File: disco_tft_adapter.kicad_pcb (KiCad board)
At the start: 4 copper layers, 127 x 60 mm, 14 parts, among them J1 QTH-030-02-L-D-A, J2 F31L-1A7H1-11030

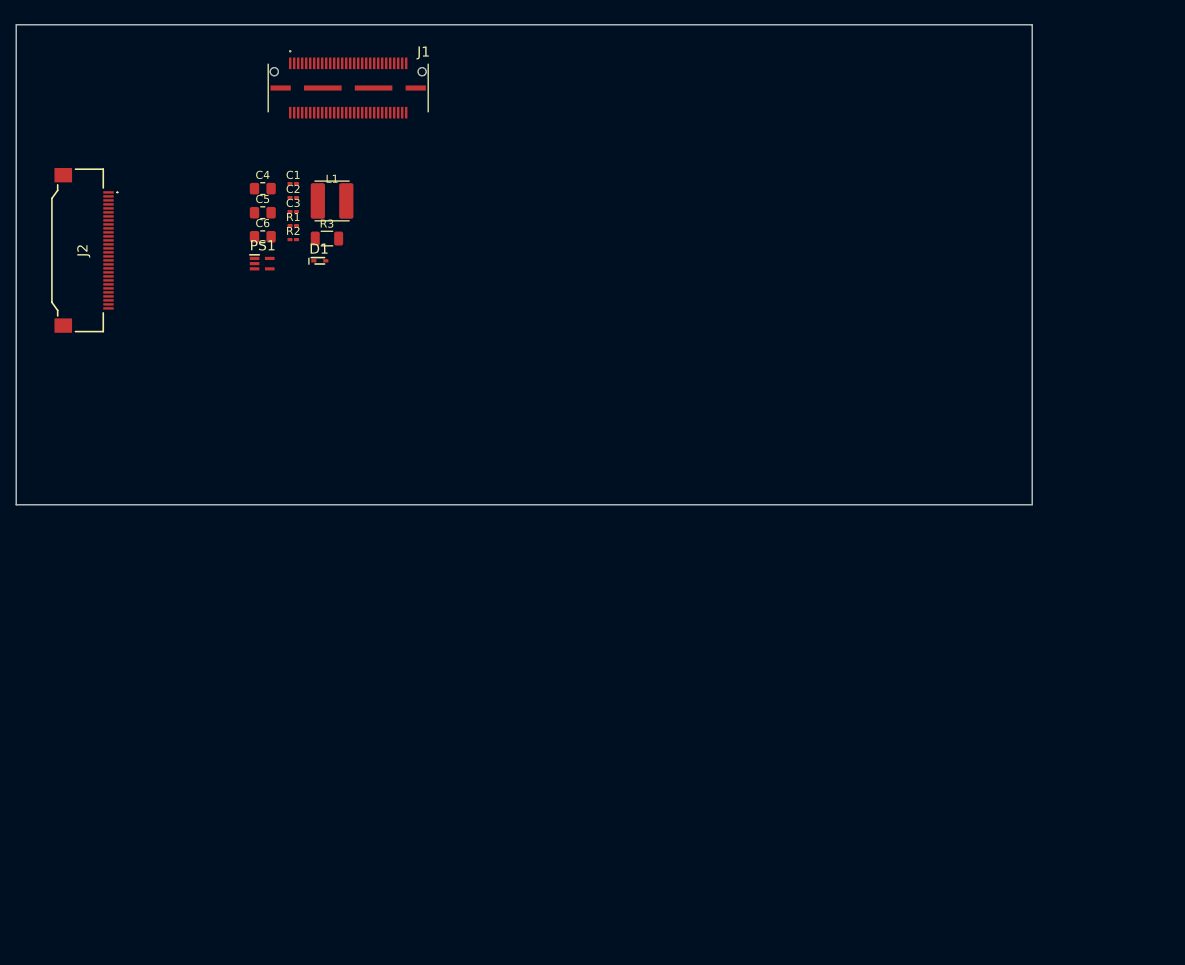
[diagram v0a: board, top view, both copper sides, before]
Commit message: [layout] add: stitching vias, planes updated, routed buck converter for LED BL, added power labels to buck converter in schematics
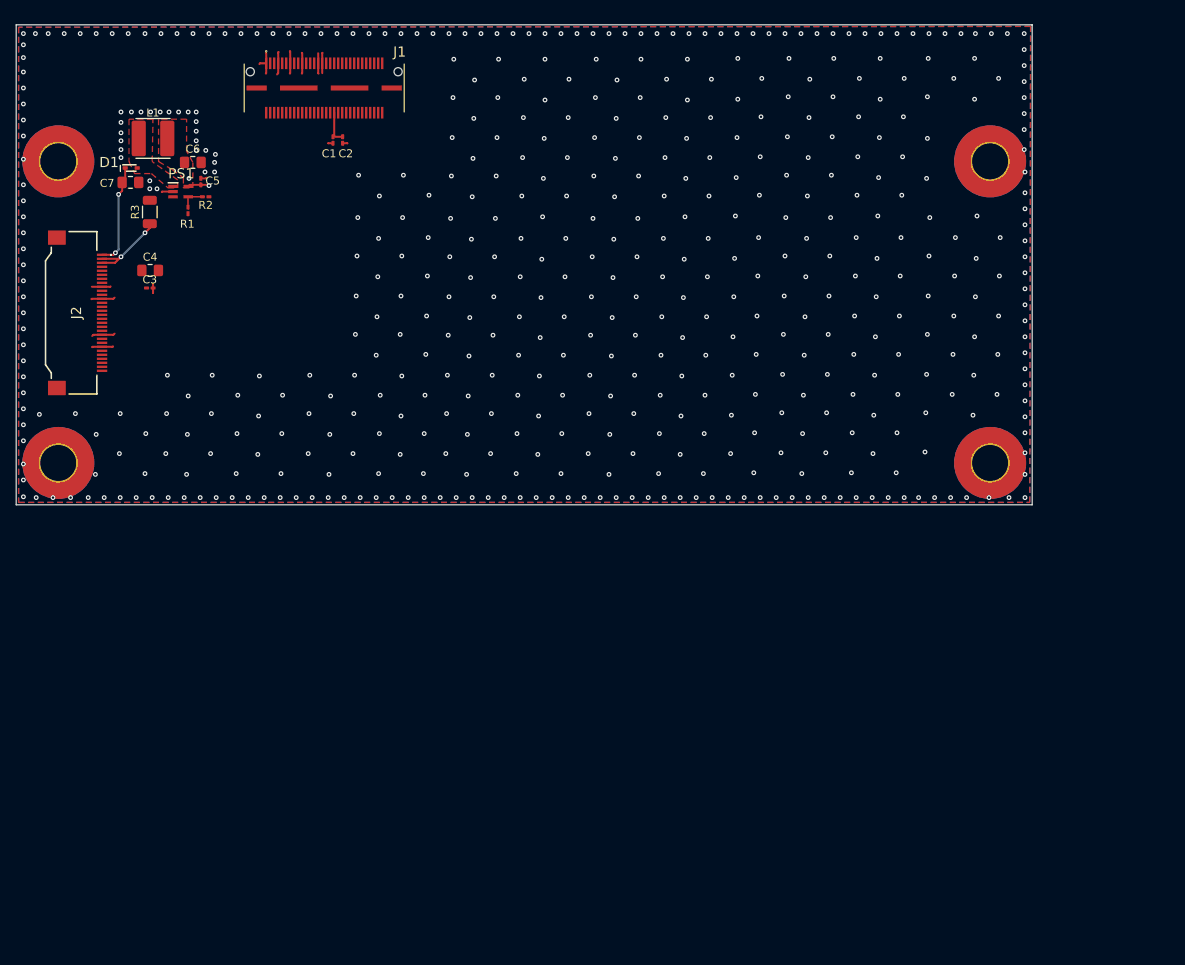
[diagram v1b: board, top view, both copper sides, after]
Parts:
- added C5: 100n, Capacitor_SMD:C_0201_0603Metric_Pad0.64x0.40mm_HandSolder, F.Cu at (45.2, 51.8)
- added H1: MountingHole_Pad, MountingHole:MountingHole_4.5mm_Pad_TopBottom, F.Cu at (27.4, 87.0)
- added H2: MountingHole_Pad, MountingHole:MountingHole_4.5mm_Pad_TopBottom, F.Cu at (27.4, 49.3)
- added H3: MountingHole_Pad, MountingHole:MountingHole_4.5mm_Pad_TopBottom, F.Cu at (143.8, 49.3)
- added H4: MountingHole_Pad, MountingHole:MountingHole_4.5mm_Pad_TopBottom, F.Cu at (143.8, 87.0)
- moved D1 26.3 mm to (36.5, 50.1)
- moved L1 23.7 mm to (39.2, 46.4), turned to 180 degrees
- moved R3 22.4 mm to (38.8, 55.6), turned to 90 degrees
- moved C3 20.3 mm to (38.8, 65.1)
- moved C7 17.9 mm to (36.4, 51.9)
- moved C4 17.4 mm to (38.8, 62.9)
- moved PS1 13.6 mm to (42.6, 53.0)
- moved R1 13.3 mm to (43.6, 55.4), turned to 90 degrees
- moved R2 12.2 mm to (45.8, 53.7), turned to 180 degrees
- moved C6 10.8 mm to (44.2, 49.4)
- moved C2 9.48 mm to (62.9, 46.6), turned to -90 degrees
- moved J2 7.84 mm to (29.3, 68.2)
- moved C1 7.37 mm to (61.7, 46.6), turned to -90 degrees
- moved J1 3.00 mm to (60.6, 40.1)
- renumbered C5 to C6, C6 to C7
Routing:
- net GND: track 0.00 -> 32.4 mm, vias 0 -> 521
- net /LEDA: track 0.00 -> 12.9 mm, vias 0 -> 2
- net /LEDK: track 0.00 -> 10.8 mm, vias 0 -> 2
- net VCC: track 0.00 -> 4.27 mm
- net Net-(PS1-CTRL): track 0.00 -> 3.07 mm
- net VCC_BL: track 0.00 -> 2.72 mm, vias 0 -> 2
- added copper zone on B.Cu, net GND
- added copper zone on F.Cu, net GND
- added copper zone on In1.Cu, net GND
- added copper zone on In2.Cu, net GND
- added copper zone on F.Cu, net Net-(D1-A)
- added copper zone on In2.Cu, net VCC
- added copper zone on F.Cu, net VCC_BL
- added copper zone on In2.Cu, net VCC_BL

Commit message: [layout] updated board shape, finished initial routing
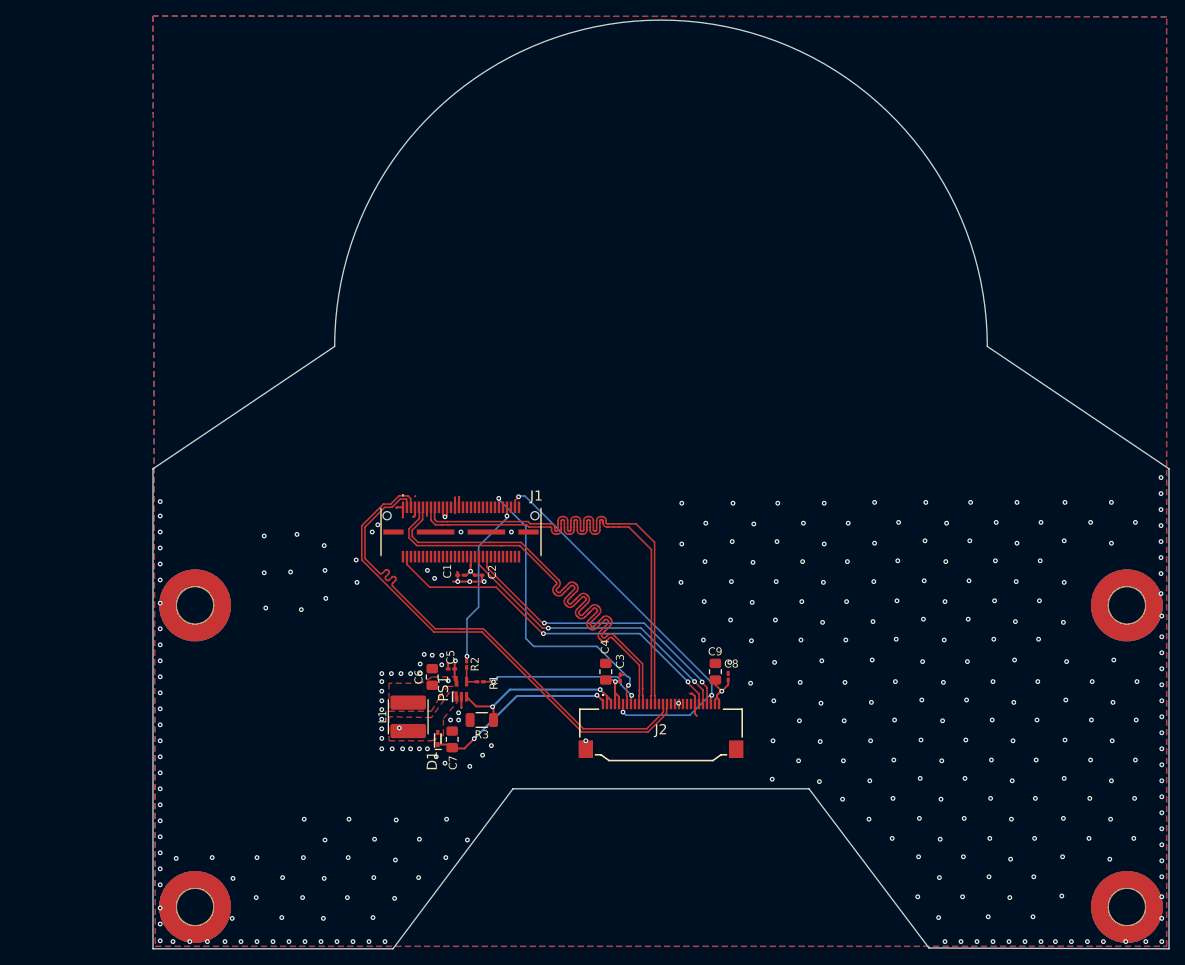
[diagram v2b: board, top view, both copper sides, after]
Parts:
- added C8: 100n, Capacitor_SMD:C_0201_0603Metric_Pad0.64x0.40mm_HandSolder, F.Cu at (111.1, 113.7)
- added C9: 4.7uF, Capacitor_SMD:C_0805_2012Metric_Pad1.18x1.45mm_HandSolder, F.Cu at (109.5, 113.1)
- moved J2 90.2 mm to (102.7, 120.6), turned to 0 degrees
- moved D1 81.0 mm to (74.8, 121.4), turned to 90 degrees
- moved C7 80.4 mm to (76.6, 121.5), turned to 90 degrees
- moved L1 79.0 mm to (71.1, 118.7), turned to -90 degrees
- moved C3 76.4 mm to (97.6, 113.9), turned to 90 degrees
- moved C4 75.9 mm to (95.8, 113.1), turned to 90 degrees
- moved R3 75.9 mm to (80.3, 119.1), turned to 180 degrees
- moved PS1 71.4 mm to (77.8, 115.2), turned to 90 degrees
- moved C6 70.9 mm to (74.1, 113.7), turned to 90 degrees
- moved R1 69.3 mm to (80.1, 114.3), turned to 180 degrees
- moved C5 68.5 mm to (76.5, 112.7), turned to 180 degrees
- moved R2 66.9 mm to (78.4, 112.1), turned to -90 degrees
- moved H1 58.1 mm to (44.5, 142.5)
- moved H2 58.1 mm to (44.5, 104.8)
- moved H3 58.1 mm to (160.9, 104.8)
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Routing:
- net /DSI_CLK_P: track 0.00 -> 62.8 mm
- net /DSI_D1_P: track 0.00 -> 62.4 mm
- net /DSI_CLK_N: track 0.00 -> 62.4 mm
- net /DSI_D1_N: track 0.00 -> 62.1 mm
- net /DSI_D0_N: track 0.00 -> 62.0 mm
- net /DSI_D0_P: track 0.00 -> 62.0 mm
- net /RST: track 0.00 -> 51.5 mm, vias 0 -> 3
- net /CTP_INT: track 0.00 -> 45.5 mm, vias 0 -> 2
- net /TE: track 0.00 -> 39.1 mm, vias 0 -> 2
- net /CTP_SCL: track 0.00 -> 37.5 mm, vias 0 -> 2
- net /CTP_SDA: track 0.00 -> 37.2 mm, vias 0 -> 2
- net /PWM_UC: track 0.00 -> 21.3 mm, vias 0 -> 2
- net /PWM_DISP: track 0.00 -> 21.2 mm, vias 0 -> 2
- net /LEDK: track 10.8 -> 23.6 mm
- net VCC: track 4.27 -> 16.6 mm, vias 0 -> 3
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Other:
- board size 127 x 60 mm -> 127 x 116.1 mm

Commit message: [layout] some adjustments, add pcb name + t3 logo
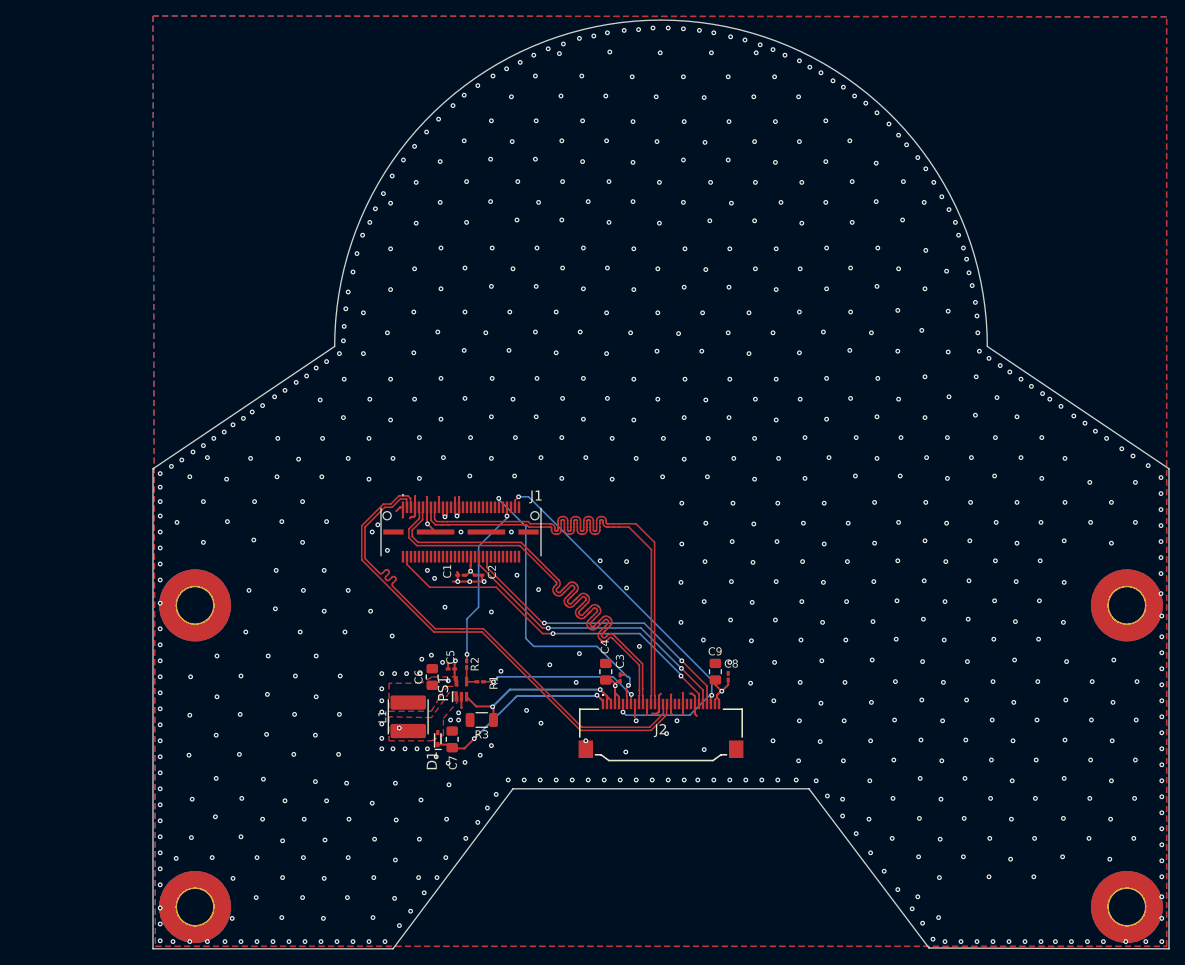
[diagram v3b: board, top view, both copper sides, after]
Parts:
- added G***: LOGO, LOGO, B.Cu at (60.3, 136.6)
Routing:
- net GND: track 20.1 -> 40.6 mm, vias 327 -> 775
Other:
- board text added: "Disco TFT Adapter Rev. A"

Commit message: [project] ready up for production, added more infos for bom
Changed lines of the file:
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@@
 			(outputformat 1)
 			(mirror no)
-			(drillshape 1)
+			(drillshape 0)
 			(scaleselection 1)
-			(outputdirectory "")
+			(outputdirectory "gerbers/")
 		)
 	)
@@
 		(tags "capacitor handsolder")
 		(property "Reference" "C2"
-			(at 1.7 -0.4 90)
+			(at 2.3 0.1 180)
 			(layer "F.SilkS")
 			(effects
@@
 			)
 		)
+		(property "Mouser Part Number" "603-C0603MRY5V9BB104"
+			(at 0 0 0)
+			(unlocked yes)
+			(layer "F.Fab")
+			(hide yes)
+			(effects
+				(font
+					(size 1 1)
+					(thickness 0.15)
+				)
+			)
+		)
 		(property ki_fp_filters "C_*")
 		(sheetname "/")
@@
 		(tags "capacitor handsolder")
 		(property "Reference" "C5"
-			(at 0.1 1.48 90)
+			(at 0.7 1.62 180)
 			(layer "F.SilkS")
 			(effects
@@
 			)
 		)
+		(property "Mouser Part Number" "603-C0603MRY5V9BB104"
+			(at 0 0 180)
+			(unlocked yes)
+			(layer "F.Fab")
+			(hide yes)
+			(effects
+				(font
+					(size 1 1)
+					(thickness 0.15)
+				)
+			)
+		)
 		(property ki_fp_filters "C_*")
 		(sheetname "/")
@@
 		(tags "capacitor handsolder")
 		(property "Reference" "C6"
-			(at 0 -1.68 90)
+			(at 0.42 -2 180)
 			(layer "F.SilkS")
 			(effects
@@
 			)
 		)
+		(property "Mouser Part Number" "581-08055D475KAT2A"
+			(at 0 0 90)
+			(unlocked yes)
+			(layer "F.Fab")
+			(hide yes)
+			(effects
+				(font
+					(size 1 1)
+					(thickness 0.15)
+				)
+			)
+		)
 		(property ki_fp_filters "C_*")
 		(sheetname "/")
@@
 			)
 		)
+		(property "Mouser Part Number" "71-CRCW12065R10FKEA"
+			(at 0 0 180)
+			(unlocked yes)
+			(layer "F.Fab")
+			(hide yes)
+			(effects
+				(font
+					(size 1 1)
+					(thickness 0.15)
+				)
+			)
+		)
 		(property ki_fp_filters "R_*")
 		(sheetname "/")
@@
 		(tags "Power Supply")
 		(property "Reference" "PS1"
-			(at 0.07 -2.25 90)
+			(at -1.35 3.35 180)
 			(layer "F.SilkS")
 			(effects
@@
 			)
 		)
+		(property "Mouser Part Number" "581-08055D475KAT2A"
+			(at 0 0 90)
+			(unlocked yes)
+			(layer "F.Fab")
+			(hide yes)
+			(effects
+				(font
+					(size 1 1)
+					(thickness 0.15)
+				)
+			)
+		)
 		(property ki_fp_filters "C_*")
 		(sheetname "/")
@@
 		(tags "resistor handsolder")
 		(property "Reference" "R1"
-			(at -1.7 -0.1 90)
+			(at -1.5 1.02 180)
 			(layer "F.SilkS")
 			(effects
@@
 			)
 		)
+		(property "Mouser Part Number" "71-RCA06030000ZSEASR"
+			(at 0 0 180)
+			(unlocked yes)
+			(layer "F.Fab")
+			(hide yes)
+			(effects
+				(font
+					(size 1 1)
+					(thickness 0.15)
+				)
+			)
+		)
 		(property ki_fp_filters "R_*")
 		(sheetname "/")
@@
 		(tags "capacitor handsolder")
 		(property "Reference" "C3"
-			(at 2.1 0 90)
+			(at 1.4625 0.6 180)
 			(layer "F.SilkS")
 			(effects
@@
 			)
 		)
+		(property "Mouser Part Number" "603-C0603MRY5V9BB104"
+			(at 0 0 90)
+			(unlocked yes)
+			(layer "F.Fab")
+			(hide yes)
+			(effects
+				(font
+					(size 1 1)
+					(thickness 0.15)
+				)
+			)
+		)
 		(property ki_fp_filters "C_*")
 		(sheetname "/")
@@
 		(tags "resistor handsolder")
 		(property "Reference" "R2"
-			(at 0 -1.05 90)
+			(at -1.02 -1.6 180)
 			(layer "F.SilkS")
 			(effects
@@
 			)
 		)
+		(property "Mouser Part Number" "71-RCA06030000ZSEASR"
+			(at 0 0 270)
+			(unlocked yes)
+			(layer "F.Fab")
+			(hide yes)
+			(effects
+				(font
+					(size 1 1)
+					(thickness 0.15)
+				)
+			)
+		)
 		(property ki_fp_filters "R_*")
 		(sheetname "/")
@@
 		(tags "capacitor handsolder")
 		(property "Reference" "C4"
-			(at 3.1 -0.1 90)
+			(at 1.5625 -2.4 180)
 			(layer "F.SilkS")
 			(effects
@@
 			)
 		)
+		(property "Mouser Part Number" "581-08055D475KAT2A"
+			(at 0 0 90)
+			(unlocked yes)
+			(layer "F.Fab")
+			(hide yes)
+			(effects
+				(font
+					(size 1 1)
+					(thickness 0.15)
+				)
+			)
+		)
 		(property ki_fp_filters "C_*")
 		(sheetname "/")
@@
 		(tags "sq")
 		(property "Reference" "L1"
-			(at 0.02 3.2 90)
+			(at -1.8 4.4 180)
 			(layer "F.SilkS")
 			(effects
@@
 			)
 		)
+		(property "Mouser Part Number" "994-LPS4018-103MRC"
+			(at 0 0 270)
+			(unlocked yes)
+			(layer "F.Fab")
+			(hide yes)
+			(effects
+				(font
+					(size 1 1)
+					(thickness 0.15)
+				)
+			)
+		)
 		(property ki_fp_filters "Choke_* *Coil* Inductor_* L_*")
 		(sheetname "/")
@@
 		(tags "capacitor handsolder")
 		(property "Reference" "C8"
-			(at 1.6075 0.4 180)
+			(at -0.1075 1.4 180)
 			(layer "F.SilkS")
 			(effects
@@
 			)
 		)
+		(property "Mouser Part Number" "603-C0603MRY5V9BB104"
+			(at 0 0 90)
+			(unlocked yes)
+			(layer "F.Fab")
+			(hide yes)
+			(effects
+				(font
+					(size 1 1)
+					(thickness 0.15)
+				)
+			)
+		)
 		(property ki_fp_filters "C_*")
 		(sheetname "/")
@@
 		(tags "capacitor handsolder")
 		(property "Reference" "C7"
-			(at -2.92 0.1 90)
+			(at -2.88 0 180)
 			(layer "F.SilkS")
 			(effects
@@
 			)
 		)
+		(property "Mouser Part Number" "603-CC805KKX5R9BB225"
+			(at 0 0 90)
+			(unlocked yes)
+			(layer "F.Fab")
+			(hide yes)
+			(effects
+				(font
+					(size 1 1)
+					(thickness 0.15)
+				)
+			)
+		)
 		(property ki_fp_filters "C_*")
 		(sheetname "/")
@@
 		(tags "capacitor handsolder")
 		(property "Reference" "C1"
-			(at 1.7 0.5 90)
+			(at 2.1 0 180)
 			(layer "F.SilkS")
 			(effects
@@
 			)
 		)
+		(property "Mouser Part Number" "603-C0603MRY5V9BB104"
+			(at 0 0 180)
+			(unlocked yes)
+			(layer "F.Fab")
+			(hide yes)
+			(effects
+				(font
+					(size 1 1)
+					(thickness 0.15)
+				)
+			)
+		)
 		(property ki_fp_filters "C_*")
 		(sheetname "/")
@@
 		(tags "Schottky Diode")
 		(property "Reference" "D1"
-			(at -2.78 -0.7 90)
+			(at -2.28 -1.5 180)
 			(layer "F.SilkS")
 			(effects
 				(font
-					(size 1.27 1.27)
-					(thickness 0.254)
+					(size 1 1)
+					(thickness 0.15)
 				)
 			)
